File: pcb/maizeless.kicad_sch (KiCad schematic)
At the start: 25 parts, among them SW1 SW_PUSH, SW10 SW_PUSH, SW11 SW_PUSH, SW12 SW_PUSH, SW13 SW_PUSH, SW14 SW_PUSH, SW15 SW_PUSH, SW16 SW_PUSH, SW17 SW_PUSH, SW18 SW_PUSH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

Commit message: Route
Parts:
- renumbered U1 to u1
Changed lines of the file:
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@@
   (symbol (lib_id "marbastlib-promicroish:nice_nano") (at 213.36 58.42 0) (unit 1)
     (in_bom no) (on_board yes) (dnp no)
-    (property "Reference" "U1" (at 213.36 40.64 0)
+    (property "Reference" "u1" (at 213.36 40.64 0)
       (effects (font (size 1.524 1.524)))
     )
@@
     (pin "29")
     (pin "27")
+    (pin "GND")
+    (pin "DIO")
+    (pin "CLK")
+    (pin "VDO")
+    (pin "boost2")
+    (pin "boost1")
     (instances
       (project "maizeless"
         (path "/da91d100-a5c8-40d4-90a3-3ae5f9c3acae"
-          (reference "U1") (unit 1)
+          (reference "u1") (unit 1)
         )
       )

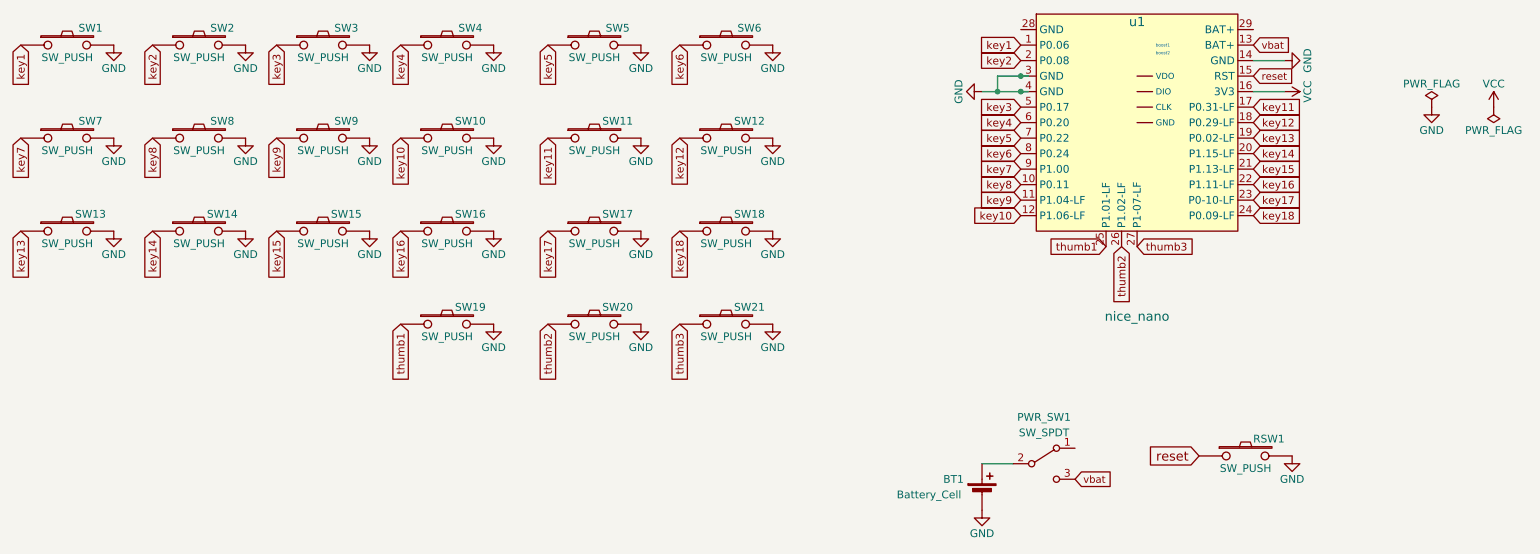
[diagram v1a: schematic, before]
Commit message: Shift thumb3, remove switch labels
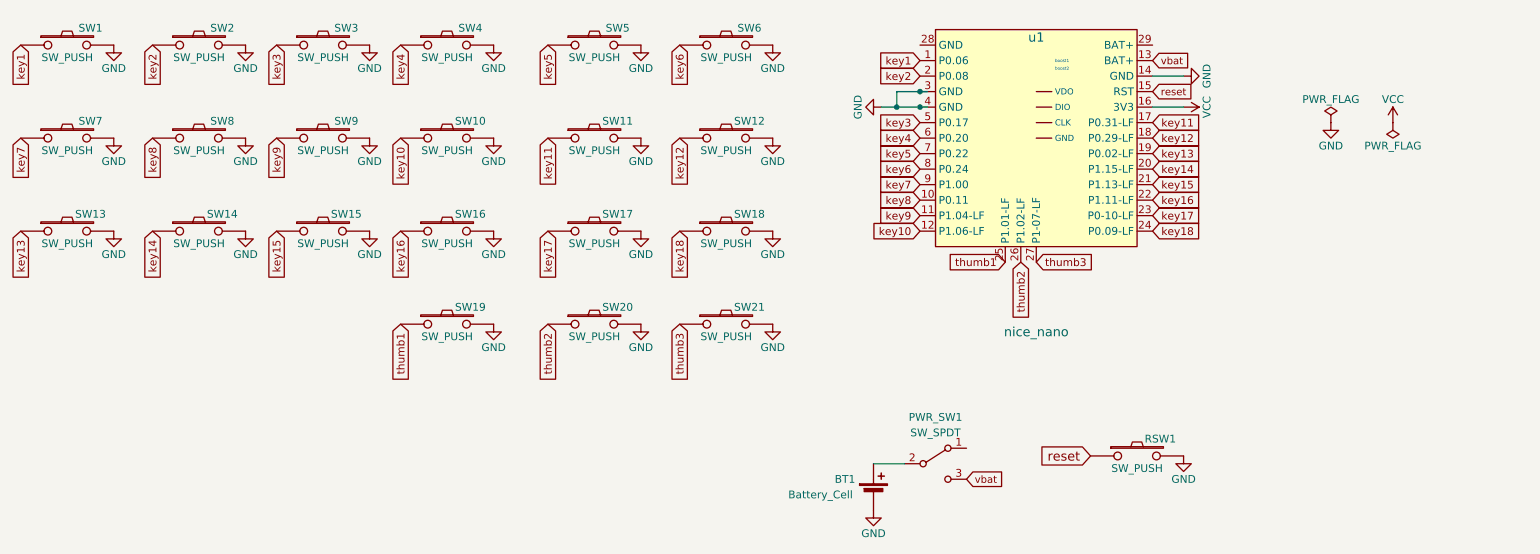
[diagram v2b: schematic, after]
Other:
- moved on the sheet: BT1, PWR_SW1, RSW1, u1

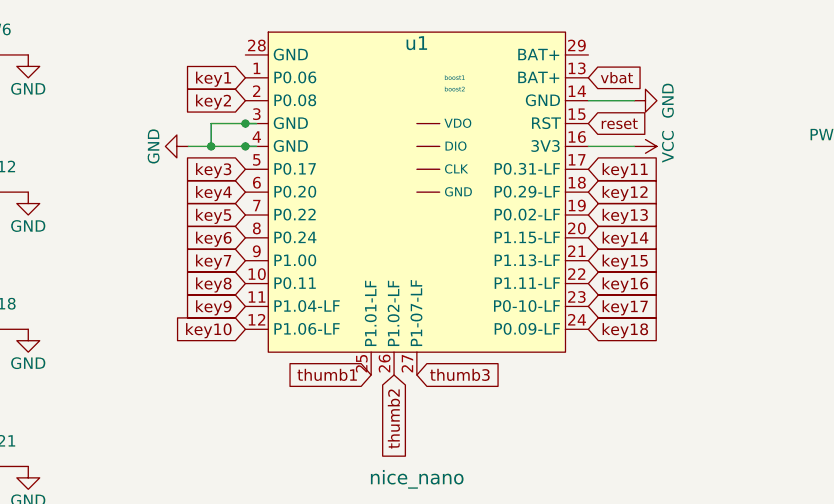
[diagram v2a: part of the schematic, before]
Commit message: Route and fix DRC errors
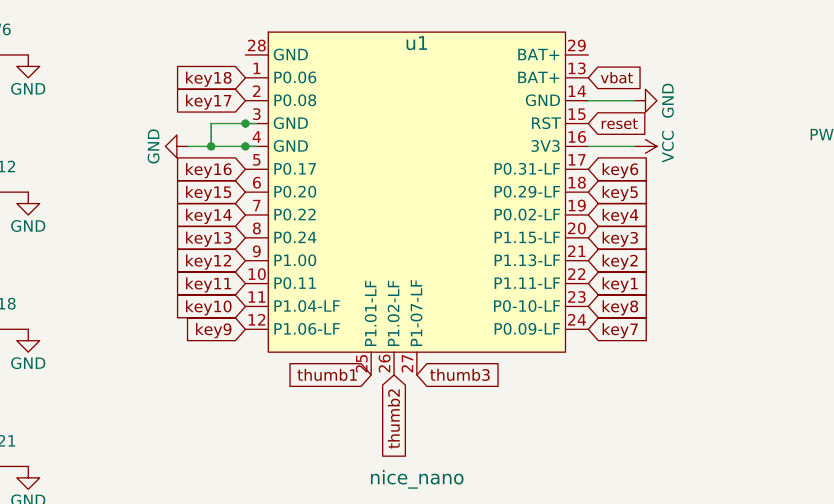
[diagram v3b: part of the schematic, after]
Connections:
- net key1: now also u1.22 (P1.11-LF); no longer u1.1 (P0.06)
- net key10: now also u1.11 (P1.04-LF); no longer u1.12 (P1.06-LF)
- net key11: now also u1.10 (P0.11); no longer u1.17 (P0.31-LF)
- net key12: now also u1.9 (P1.00); no longer u1.18 (P0.29-LF)
- net key13: now also u1.8 (P0.24); no longer u1.19 (P0.02-LF)
- net key14: now also u1.7 (P0.22); no longer u1.20 (P1.15-LF)
- net key15: now also u1.6 (P0.20); no longer u1.21 (P1.13-LF)
- net key16: now also u1.5 (P0.17); no longer u1.22 (P1.11-LF)
- net key17: now also u1.2 (P0.08); no longer u1.23 (P0-10-LF)
- net key18: now also u1.1 (P0.06); no longer u1.24 (P0.09-LF)
- net key2: now also u1.21 (P1.13-LF); no longer u1.2 (P0.08)
- net key3: now also u1.20 (P1.15-LF); no longer u1.5 (P0.17)
- net key4: now also u1.19 (P0.02-LF); no longer u1.6 (P0.20)
- net key5: now also u1.18 (P0.29-LF); no longer u1.7 (P0.22)
- net key6: now also u1.17 (P0.31-LF); no longer u1.8 (P0.24)
- net key7: now also u1.24 (P0.09-LF); no longer u1.9 (P1.00)
- net key8: now also u1.23 (P0-10-LF); no longer u1.10 (P0.11)
- net key9: now also u1.12 (P1.06-LF); no longer u1.11 (P1.04-LF)

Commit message: Re-route for nicer looking traces; fix missing ground
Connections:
- net GND: now also u1.28 (GND)
- net vbat: now also u1.29 (BAT+)
- no-connect marks 0 -> 1
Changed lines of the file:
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@@
   (junction (at 173.99 54.61) (diameter 0) (color 0 0 0 0)
   )
+  (no_connect (at 185.42 110.49))
   (wire (pts (xy 173.99 54.61) (xy 177.8 54.61))
     (stroke (width 0) (type default))
@@
   )
   (wire (pts (xy 171.45 54.61) (xy 173.99 54.61))
+    (stroke (width 0) (type default))
+  )
+  (wire (pts (xy 171.45 44.45) (xy 177.8 44.45))
     (stroke (width 0) (type default))
   )
@@
     (property "Intersheetrefs" "${INTERSHEET_REFS}" (at 169.6896 57.15 0)
       (effects (font (size 1.27 1.27)) (justify right) hide)
+    )
+  )
+  (global_label "vbat" (shape input) (at 215.9 44.45 0)
+    (effects (font (size 1.1938 1.1938)) (justify left))
+    (property "Intersheetrefs" "${INTERSHEET_REFS}" (at 215.9 44.45 0)
+      (effects (font (size 1.27 1.27)) hide)
     )
   )
@@
         )
       )
+    )
+  )
+  (symbol (lib_id "power:GND") (at 171.45 44.45 270) (unit 1)
+    (in_bom yes) (on_board yes) (dnp no)
+    (property "Reference" "#PWR029" (at 165.1 44.45 0)
+      (effects (font (size 1.27 1.27)) hide)
+    )
+    (property "Value" "GND" (at 167.64 44.45 0)
+      (effects (font (size 1.27 1.27)))
+    )
+    (property "Footprint" "" (at 171.45 44.45 0)
+      (effects (font (size 1.27 1.27)) hide)
+    )
+    (property "Datasheet" "" (at 171.45 44.45 0)
+      (effects (font (size 1.27 1.27)) hide)
+    )
+    (pin "1")
+    (instances
+      (project "maizeless"
+        (path "/da91d100-a5c8-40d4-90a3-3ae5f9c3acae"
+          (reference "#PWR029") (unit 1)
+        )
+      )

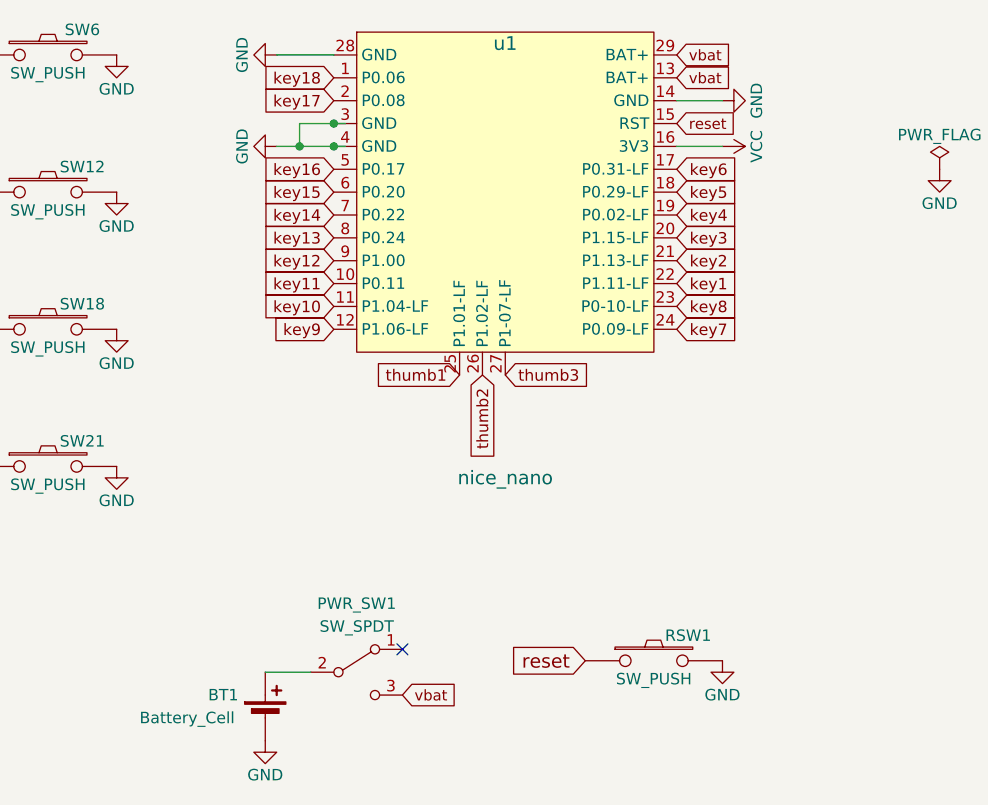
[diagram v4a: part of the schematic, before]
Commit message: Fix ERC rules by setting gnd pins to input
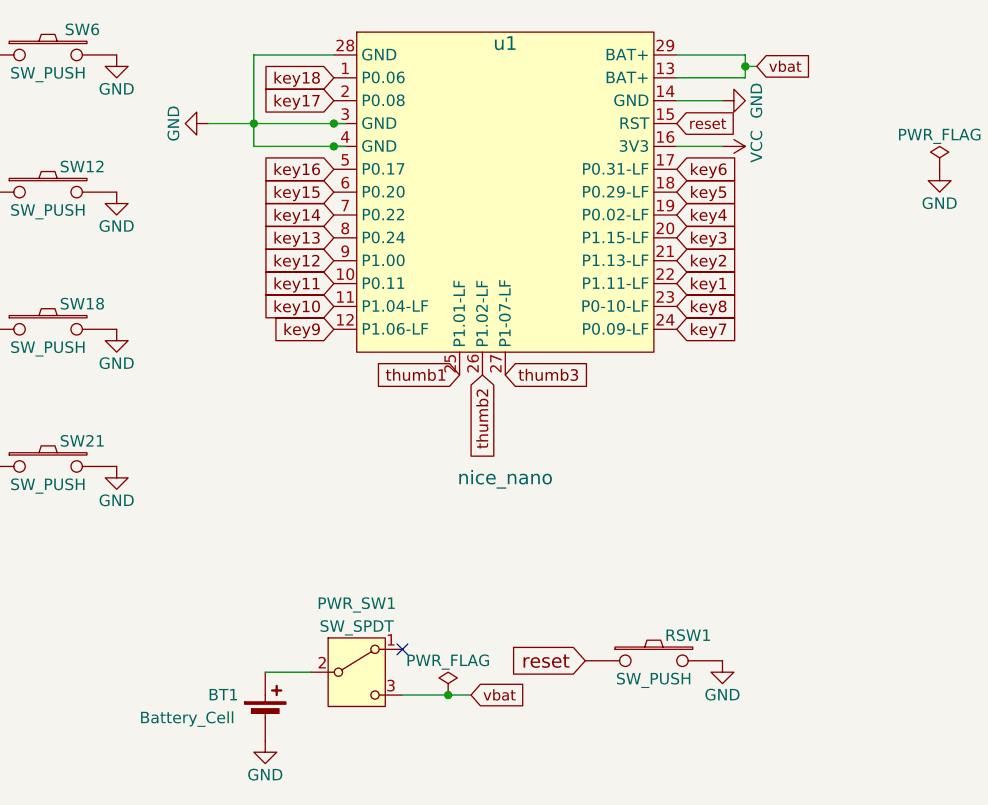
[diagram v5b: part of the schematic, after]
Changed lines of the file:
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@@
   (junction (at 177.8 52.07) (diameter 0) (color 0 0 0 0)
   )
+  (junction (at 168.91 52.07) (diameter 0) (color 0 0 0 0)
+  )
   (junction (at 177.8 54.61) (diameter 0) (color 0 0 0 0)
   )
-  (junction (at 173.99 54.61) (diameter 0) (color 0 0 0 0)
+  (junction (at 223.52 45.72) (diameter 0) (color 0 0 0 0)
+  )
+  (junction (at 190.5 115.57) (diameter 0) (color 0 0 0 0)
   )
   (no_connect (at 185.42 110.49))
-  (wire (pts (xy 173.99 54.61) (xy 177.8 54.61))
+  (wire (pts (xy 185.42 115.57) (xy 190.5 115.57))
+    (stroke (width 0) (type default))
+  )
+  (wire (pts (xy 168.91 54.61) (xy 177.8 54.61))
+    (stroke (width 0) (type default))
+  )
+  (wire (pts (xy 168.91 52.07) (xy 168.91 54.61))
+    (stroke (width 0) (type default))
+  )
+  (wire (pts (xy 223.52 45.72) (xy 223.52 44.45))
     (stroke (width 0) (type default))
   )
@@
     (stroke (width 0) (type default))
   )
-  (wire (pts (xy 173.99 52.07) (xy 177.8 52.07))
-    (stroke (width 0) (type default))
-  )
-  (wire (pts (xy 171.45 54.61) (xy 173.99 54.61))
-    (stroke (width 0) (type default))
-  )
-  (wire (pts (xy 171.45 44.45) (xy 177.8 44.45))
+  (wire (pts (xy 224.79 45.72) (xy 223.52 45.72))
+    (stroke (width 0) (type default))
+  )
+  (wire (pts (xy 193.04 115.57) (xy 190.5 115.57))
+    (stroke (width 0) (type default))
+  )
+  (wire (pts (xy 168.91 52.07) (xy 168.91 44.45))
+    (stroke (width 0) (type default))
+  )
+  (wire (pts (xy 168.91 52.07) (xy 177.8 52.07))
+    (stroke (width 0) (type default))
+  )
+  (wire (pts (xy 215.9 46.99) (xy 223.52 46.99))
+    (stroke (width 0) (type default))
+  )
+  (wire (pts (xy 163.83 52.07) (xy 168.91 52.07))
+    (stroke (width 0) (type default))
+  )
+  (wire (pts (xy 223.52 46.99) (xy 223.52 45.72))
+    (stroke (width 0) (type default))
+  )
+  (wire (pts (xy 223.52 44.45) (xy 215.9 44.45))
     (stroke (width 0) (type default))
   )
@@
     (stroke (width 0) (type default))
   )
+  (wire (pts (xy 168.91 44.45) (xy 177.8 44.45))
+    (stroke (width 0) (type default))
+  )
   (wire (pts (xy 170.18 113.03) (xy 175.26 113.03))
     (stroke (width 0) (type default))
   )
   (wire (pts (xy 177.8 52.07) (xy 179.07 52.07))
-    (stroke (width 0) (type default))
-  )
-  (wire (pts (xy 173.99 52.07) (xy 173.99 54.61))
     (stroke (width 0) (type default))
   )
@@
     )
   )
-  (global_label "vbat" (shape input) (at 215.9 46.99 0)
-    (effects (font (size 1.1938 1.1938)) (justify left))
-    (property "Intersheetrefs" "${INTERSHEET_REFS}" (at 215.9 46.99 0)
-      (effects (font (size 1.27 1.27)) hide)
-    )
-  )
   (global_label "key14" (shape input) (at 177.8 62.23 180) (fields_autoplaced)
     (effects (font (size 1.27 1.27)) (justify right))
@@
     )
   )
-  (global_label "vbat" (shape input) (at 185.42 115.57 0)
+  (global_label "vbat" (shape input) (at 193.04 115.57 0)
     (effects (font (size 1.1938 1.1938)) (justify left))
-    (property "Intersheetrefs" "${INTERSHEET_REFS}" (at 185.42 115.57 0)
+    (property "Intersheetrefs" "${INTERSHEET_REFS}" (at 193.04 115.57 0)
       (effects (font (size 1.27 1.27)) hide)
     )
@@
     )
   )
-  (global_label "vbat" (shape input) (at 215.9 44.45 0)
+  (global_label "vbat" (shape input) (at 224.79 45.72 0)
     (effects (font (size 1.1938 1.1938)) (justify left))
-    (property "Intersheetrefs" "${INTERSHEET_REFS}" (at 215.9 44.45 0)
+    (property "Intersheetrefs" "${INTERSHEET_REFS}" (at 224.79 45.72 0)
       (effects (font (size 1.27 1.27)) hide)
     )
@@
     )
   )
-  (symbol (lib_id "power:GND") (at 171.45 54.61 270) (unit 1)
-    (in_bom yes) (on_board yes) (dnp no)
-    (property "Reference" "#PWR04" (at 165.1 54.61 0)
-      (effects (font (size 1.27 1.27)) hide)
-    )
-    (property "Value" "GND" (at 167.64 54.61 0)
-      (effects (font (size 1.27 1.27)))
-    )
-    (property "Footprint" "" (at 171.45 54.61 0)
-      (effects (font (size 1.27 1.27)) hide)
-    )
-    (property "Datasheet" "" (at 171.45 54.61 0)
+  (symbol (lib_id "power:GND") (at 163.83 52.07 270) (unit 1)
+    (in_bom yes) (on_board yes) (dnp no)
+    (property "Reference" "#PWR04" (at 157.48 52.07 0)
+      (effects (font (size 1.27 1.27)) hide)
+    )
+    (property "Value" "GND" (at 160.02 52.07 0)
+      (effects (font (size 1.27 1.27)))
+    )
+    (property "Footprint" "" (at 163.83 52.07 0)
+      (effects (font (size 1.27 1.27)) hide)
+    )
+    (property "Datasheet" "" (at 163.83 52.07 0)
       (effects (font (size 1.27 1.27)) hide)
     )
@@
         (path "/da91d100-a5c8-40d4-90a3-3ae5f9c3acae"
           (reference "SW13") (unit 1)
+        )
+      )
+    )
+  )
+  (symbol (lib_id "power:PWR_FLAG") (at 190.5 115.57 0) (unit 1)
+    (in_bom yes) (on_board yes) (dnp no)
+    (property "Reference" "#FLG03" (at 190.5 113.665 0)
+      (effects (font (size 1.27 1.27)) hide)
+    )
+    (property "Value" "PWR_FLAG" (at 190.5 111.76 0)
+      (effects (font (size 1.27 1.27)))
+    )
+    (property "Footprint" "" (at 190.5 115.57 0)
+      (effects (font (size 1.27 1.27)) hide)
+    )
+    (property "Datasheet" "" (at 190.5 115.57 0)
+      (effects (font (size 1.27 1.27)) hide)
+    )
+    (pin "1")
+    (instances
+      (project "maizeless"
+        (path "/da91d100-a5c8-40d4-90a3-3ae5f9c3acae"
+          (reference "#FLG03") (unit 1)
         )
       )
@@
         )
       )
-    )
-  )
-  (symbol (lib_id "power:GND") (at 171.45 44.45 270) (unit 1)
-    (in_bom yes) (on_board yes) (dnp no)
-    (property "Reference" "#PWR029" (at 165.1 44.45 0)
-      (effects (font (size 1.27 1.27)) hide)
-    )
-    (property "Value" "GND" (at 167.64 44.45 0)
-      (effects (font (size 1.27 1.27)))
-    )
-    (property "Footprint" "" (at 171.45 44.45 0)
-      (effects (font (size 1.27 1.27)) hide)
-    )
-    (property "Datasheet" "" (at 171.45 44.45 0)
-      (effects (font (size 1.27 1.27)) hide)
-    )
-    (pin "1")
-    (instances
-      (project "maizeless"
-        (path "/da91d100-a5c8-40d4-90a3-3ae5f9c3acae"
-          (reference "#PWR029") (unit 1)
-        )
-      )
